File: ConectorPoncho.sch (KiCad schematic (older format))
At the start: 2 parts

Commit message: Se completaron los circuitos esquematicos, falta revision.
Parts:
- removed XA?: Conn_Poncho2P_2x_20x2, symbol Conn_Poncho2P_2x_20x2
- added unit 1 of XA1
- gave numbers to parts that had none: 1
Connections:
- net +5VP is gone; now on net +5V: XA1.42 (+5V)
- net GNDD is gone; now on net GND: XA1.43 (GND), XA1.45 (GND), XA1.47 (GND), XA1.51 (GND), XA1.53 (GND), XA1.57 (GND), XA1.59 (GND), XA1.65 (GND), XA1.67 (GND), XA1.77 (GND), XA1.79 (GND)
- net +3.3VP: now also XA1.1 (+3.3V)
- net +5V: now also XA1.2 (+5V)
- net GND: now also XA1.20 (GND), XA1.22 (GND), XA1.24 (GND), XA1.26 (GND), XA1.28 (GND), XA1.30 (GND), XA1.32 (GND), XA1.38 (GND), XA1.4 (GND), XA1.40 (GND)
- net GNDA: now also XA1.10 (GNDA), XA1.12 (GNDA), XA1.14 (GNDA), XA1.16 (GNDA), XA1.18 (GNDA), XA1.7 (GNDA), XA1.8 (GNDA)
- net GPIO0: now also XA1.39 (tecCOL0); no longer XA1.69 (GPIO0)
- net GPIO1: now also XA1.31 (tecCOL1); no longer XA1.72 (GPIO1)
- net Pote: now also XA1.13 (ADC1)
- new net Buzzer: XA1.15 (DAC)
- new net CNY_IN: XA1.34 (tecCOL2)
- new net Encoder_A: XA1.33 (tecF0)
- new net Encoder_B: XA1.36 (tecF1)
- new net OPTO_IN0: XA1.37 (tecF2)
- new net OPTO_IN1: XA1.35 (tecF3)
- no-connect marks 45 -> 39
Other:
- note added: "P1\n"
- note added: "P2\n"
- moved on the sheet: XA1B

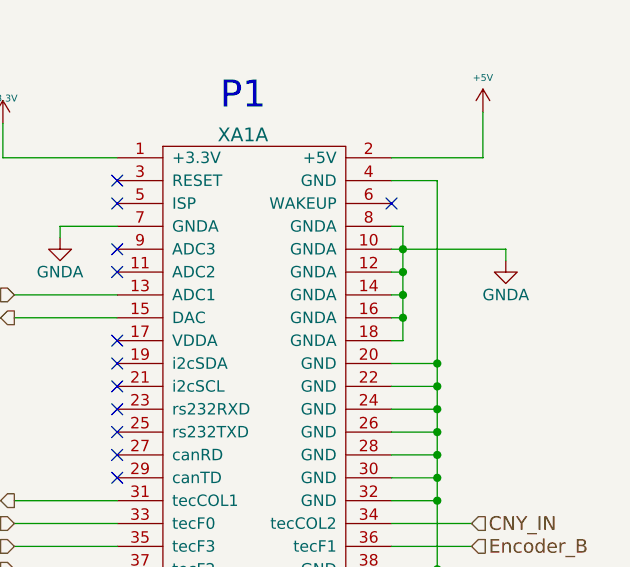
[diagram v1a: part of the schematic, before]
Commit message: se agregaron casi todos los footprint faltan el conector del poncho, encoder y CNY70
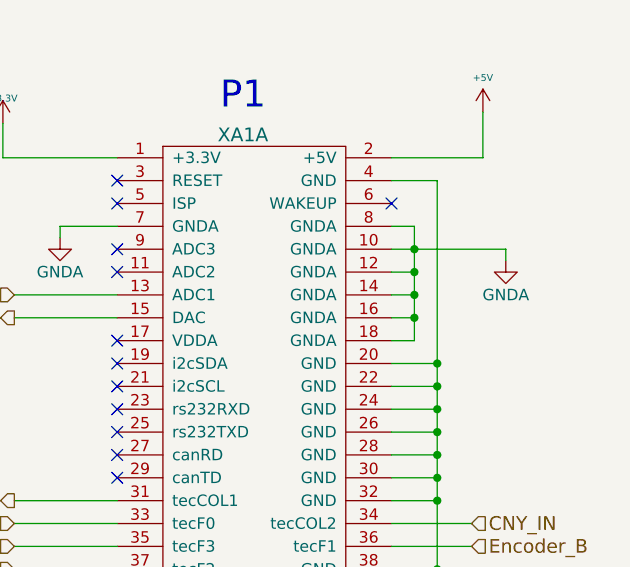
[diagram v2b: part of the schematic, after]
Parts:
- XA1: footprint footprint:Conn_Poncho_SinBorde -> (none)
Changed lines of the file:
@@
 EESchema Schematic File Version 2
 LIBS:device
-LIBS:dsp
 LIBS:power
 LIBS:sensors
@@
 LIBS:switches
 LIBS:references
-LIBS:maxim
-LIBS:atmel
-LIBS:motorola
 LIBS:interface
 LIBS:cmos_ieee
 LIBS:analog_devices
 LIBS:nordicsemi
-LIBS:microchip_pic32mcu
 LIBS:74xgxx
 LIBS:transistors
-LIBS:philips
 LIBS:nxp_armmcu
-LIBS:supertex
 LIBS:logo
 LIBS:Power_Management
@@
 LIBS:contrib
 LIBS:cmos4000
-LIBS:ac-dc
-LIBS:memory
-LIBS:digital-audio
-LIBS:rfcom
-LIBS:video
-LIBS:microchip_pic16mcu
-LIBS:microchip_pic10mcu
-LIBS:onsemi
-LIBS:brooktre
-LIBS:Oscillators
-LIBS:stm32
 LIBS:elec-unifil
 LIBS:graphic
 LIBS:display
-LIBS:intel
-LIBS:Zilog
 LIBS:dc-dc
-LIBS:ftdi
-LIBS:microchip_pic18mcu
-LIBS:msp430
-LIBS:hc11
-LIBS:Lattice
-LIBS:cypress
-LIBS:Xicor
-LIBS:silabs
-LIBS:microchip
 LIBS:opto
 LIBS:transf
@@
 LIBS:pspice
 LIBS:xilinx
-LIBS:Symbols_EN60617_13Mar2013
-LIBS:Symbols_EN60617-10_HF-Radio_DRAFT_12Sep2013
-LIBS:Symbols_Transformer-Diskrete_RevA
-LIBS:Symbols_ICs-Diskrete_RevD10
-LIBS:Symbols_ICs-Opto_RevB_16Sep2013
-LIBS:Symbols_Socket-DIN41612_RevA
-LIBS:Symbols_DCDC-ACDC-Converter_RevC_20Jul2012
-LIBS:Symbols_Microcontroller_Philips-NXP_RevA_06Oct2013
-LIBS:SymbolsSimilarEN60617+oldDIN617-RevE8
 LIBS:w_device
 LIBS:tvs
@@
 LIBS:pbss5240xf
 LIBS:nsi50010yt1g
-LIBS:net-phy
 LIBS:mcu-st
-LIBS:mcu-nxp
-LIBS:mcp1416
-LIBS:mcp1415
-LIBS:lm2596
-LIBS:g5v2
 LIBS:fqt13n06l
 LIBS:bat54_c
-LIBS:audio-vlsi
-LIBS:amesser-usb
 LIBS:amesser-power
 LIBS:amesser-linear
@@
 LIBS:amesser-ad
 LIBS:Transil_diode
-LIBS:TXB0108
-LIBS:TJA1040
-LIBS:Si50x
-LIBS:SCHA5B0200
 LIBS:PS2805
-LIBS:PRTR5V0U2X
-LIBS:PBSS5240
-LIBS:MIC2025
-LIBS:LPC4337JBD144
-LIBS:IS42S16400F
-LIBS:FT2232H
 LIBS:BLM15HG6015N1D
 LIBS:93CXX
@@
 F 0 "XA1" H 4350 3100 60  0000 C CNN
 F 1 "Conn_Poncho2P_2x_20x2" H 4400 1000 60  0000 C CNN
-F 2 "" H 4050 2700 60  0000 C CNN
+F 2 "" H 4050 2700 60  0001 C CNN
 F 3 "" H 4050 2700 60  0000 C CNN
 	2    4050 2700
@@
 Wire Wire Line
 	5250 2300 5250 2400
-Wire Wire Line
-	5250 2400 5000 2400
 Wire Wire Line
 	3800 2500 3450 2500
@@
 F 0 "XA1" H 7950 3100 60  0000 C CNN
 F 1 "Conn_Poncho2P_2x_20x2" H 8000 1000 60  0000 C CNN
-F 2 "footprint:Conn_Poncho_SinBorde" H 7650 2700 60  0001 C CNN
+F 2 "" H 7650 2700 60  0001 C CNN
 F 3 "" H 7650 2700 60  0000 C CNN
 F 4 "Harwin" H 7650 2700 60  0001 C CNN "Manf"
@@
 	7150 2700 7150 2750
 Wire Wire Line
-	8600 2700 8650 2700
-Wire Wire Line
-	8650 2700 8650 3200
-Wire Wire Line
-	8650 3200 8600 3200
-Wire Wire Line
-	8600 3100 8650 3100
-Connection ~ 8650 3100
-Wire Wire Line
-	8600 3000 8650 3000
-Connection ~ 8650 3000
-Wire Wire Line
-	8600 2900 8650 2900
-Connection ~ 8650 2900
-Wire Wire Line
-	8600 2800 9100 2800
-Connection ~ 8650 2800
-Wire Wire Line
-	9100 2800 9100 2850
+	8600 2700 8700 2700
+Wire Wire Line
+	8700 3200 8600 3200
+Wire Wire Line
+	8600 3100 8700 3100
+Wire Wire Line
+	8600 3000 8700 3000
+Wire Wire Line
+	8600 2900 8700 2900
 Wire Wire Line
 	6900 2400 6900 2250
@@
 Wire Wire Line
 	8950 4000 8600 4000
+Wire Wire Line
+	5250 2400 5000 2400
+Wire Wire Line
+	8600 2800 9100 2800
+Wire Wire Line
+	9100 2800 9100 2850
+Wire Wire Line
+	8700 2700 8700 3200
+Connection ~ 8700 2800
+Connection ~ 8700 2900
+Connection ~ 8700 3000
+Connection ~ 8700 3100
 $EndSCHEMATC

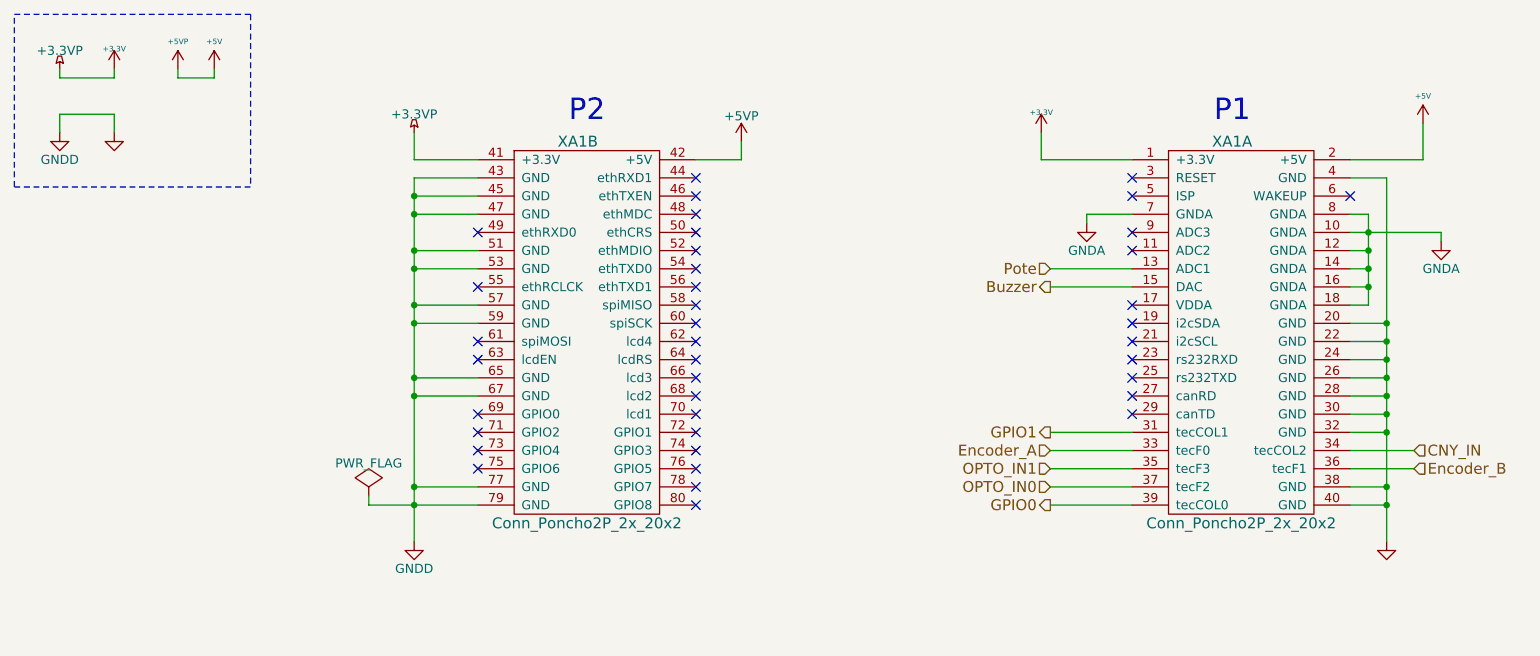
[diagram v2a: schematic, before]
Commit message: Correcion de errores, asignacion de footprints y ubicacion prelimilar de componentes.
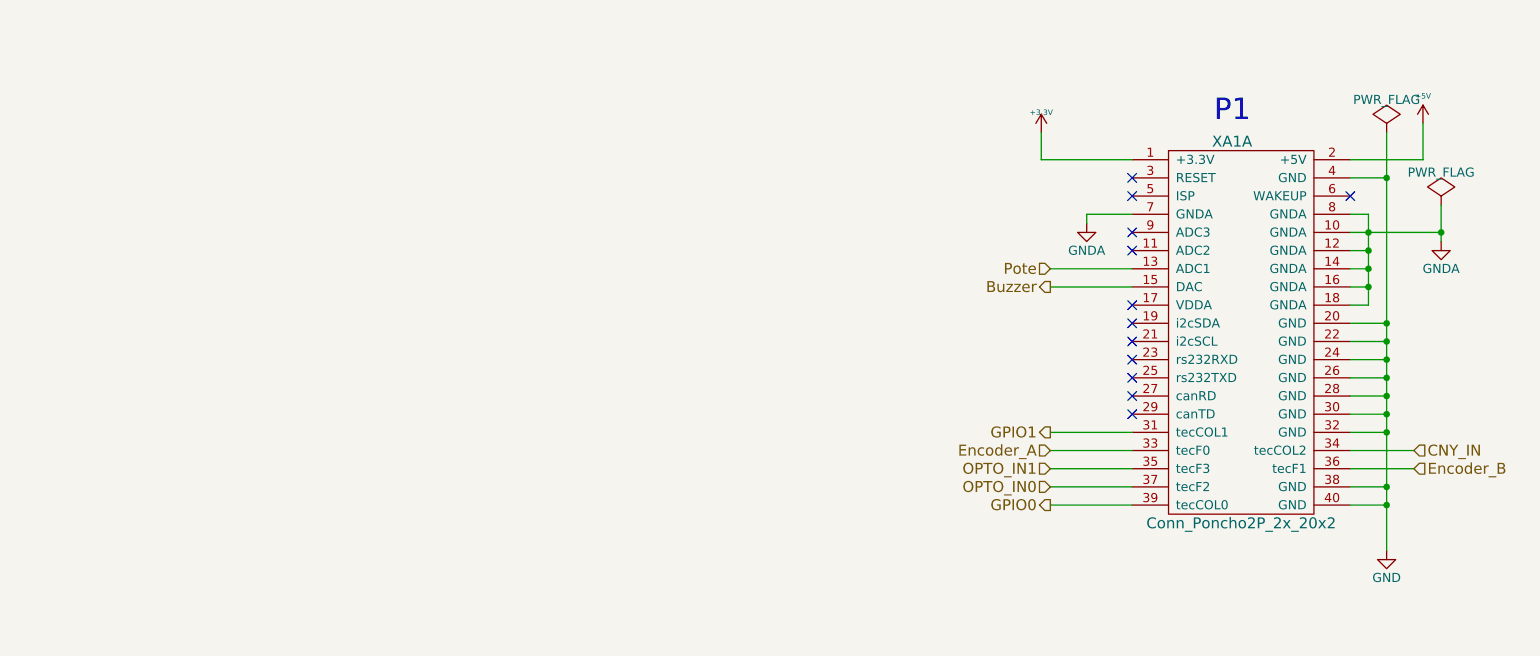
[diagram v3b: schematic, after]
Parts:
- removed unit 2 of XA1
- XA1: footprint (none) -> footprint:Conn_Poncho_Derecha
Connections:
- net +3.3VP renamed +3V3
- no-connect marks 39 -> 12
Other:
- note removed: "P2\n"

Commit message: Se definió contorno de la placa y se ubicaron los componentes. También se ruteo la placa completa, falta revisión
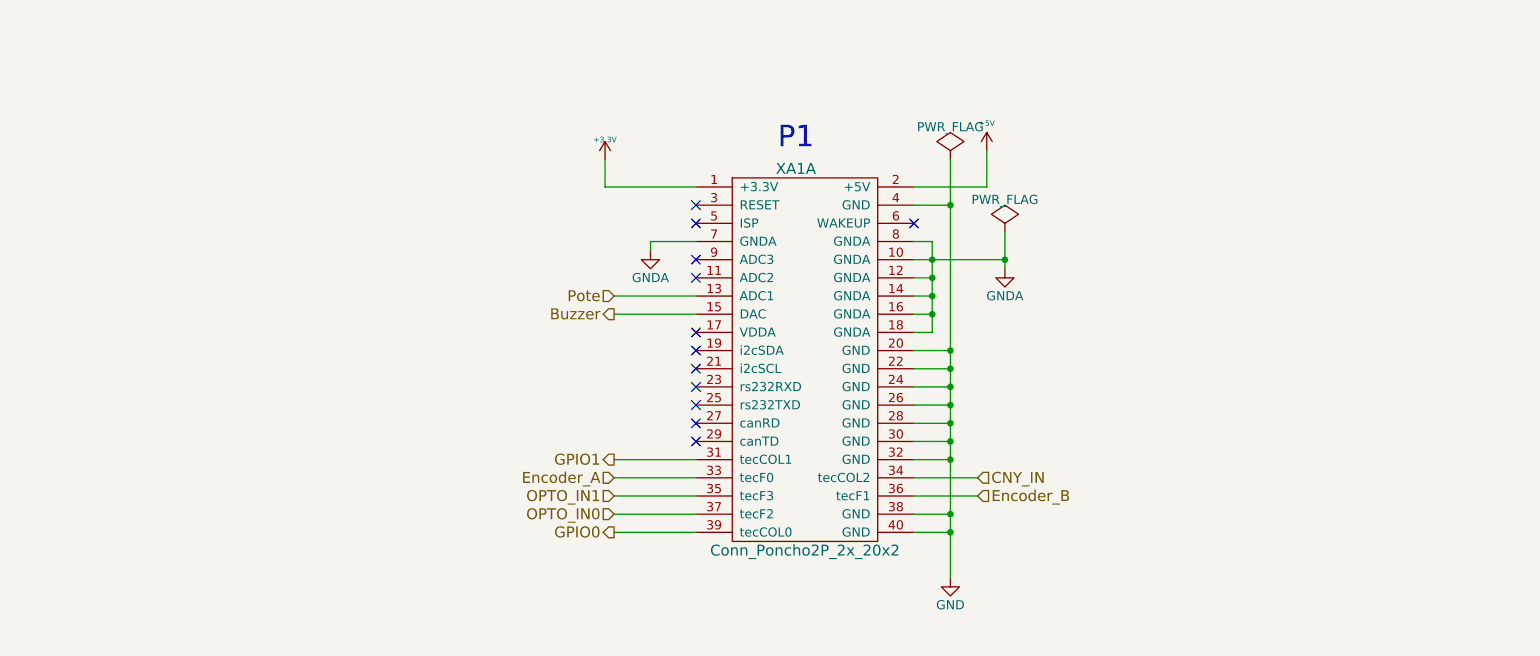
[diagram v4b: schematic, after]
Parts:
- XA1: footprint footprint:Conn_Poncho_Derecha -> footprint:Conn_Poncho_Derecha_SinBorde
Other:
- moved on the sheet: XA1A

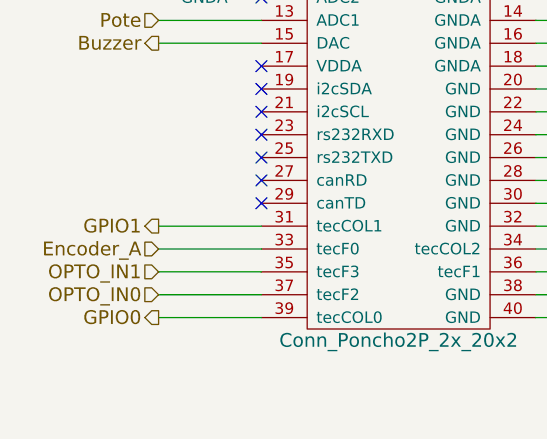
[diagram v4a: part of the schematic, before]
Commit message: Reubicacion de optoacopladores, cambio de footoprins de resistencias a 0805, correcion general.Falta arreglar archivos vista 3d y completar los campos #digikey
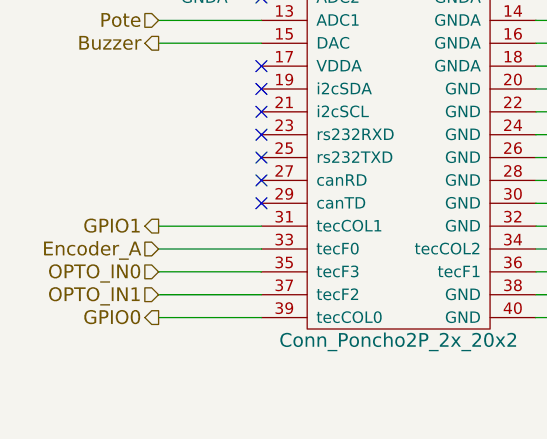
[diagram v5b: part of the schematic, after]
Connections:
- net OPTO_IN0: now also XA1.35 (tecF3); no longer XA1.37 (tecF2)
- net OPTO_IN1: now also XA1.37 (tecF2); no longer XA1.35 (tecF3)
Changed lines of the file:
@@
 EESchema Schematic File Version 2
-LIBS:power
 LIBS:EduPoncho-cache
 EELAYER 25 0
@@
 Comment2 "Autores y Licencia del modelo (Diego Brengi - UNLaM)"
 Comment3 "Autor del poncho (Evangelista Guillermo). Ver directorio \"doc\""
-Comment4 ""
+Comment4 "Revisor: Martinez Horacio"
 $EndDescr
 Text HLabel 4550 4450 0    60   Output ~ 0
@@
 Encoder_B
 Text HLabel 4550 4350 0    60   Input ~ 0
-OPTO_IN0
-Text HLabel 4550 4250 0    60   Input ~ 0
 OPTO_IN1
 Wire Wire Line
 	5000 4150 4550 4150
-Wire Wire Line
-	4550 4250 5000 4250
 Wire Wire Line
 	5000 4350 4550 4350
@@
 $EndComp
 Connection ~ 6400 2650
+Text HLabel 4550 4250 0    60   Input ~ 0
+OPTO_IN0
+Wire Wire Line
+	5000 4250 4550 4250
 $EndSCHEMATC
